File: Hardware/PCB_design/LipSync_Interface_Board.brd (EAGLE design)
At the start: 69.8 x 63.5 mm, 31 parts, among them T1 2N3906, U2 SF_MATE_RN42, U3 MPXV7002

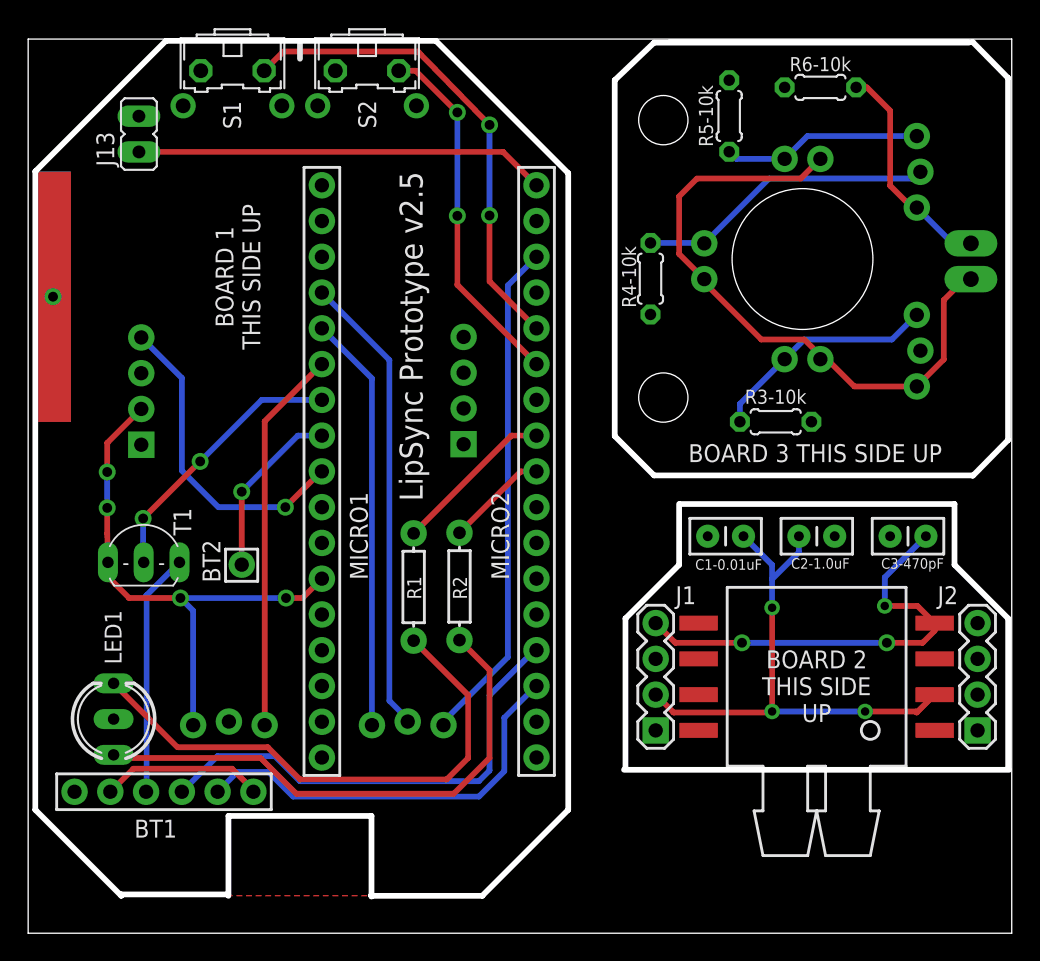
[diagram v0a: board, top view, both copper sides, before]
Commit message: Updated PCB eagle files to version 2.7
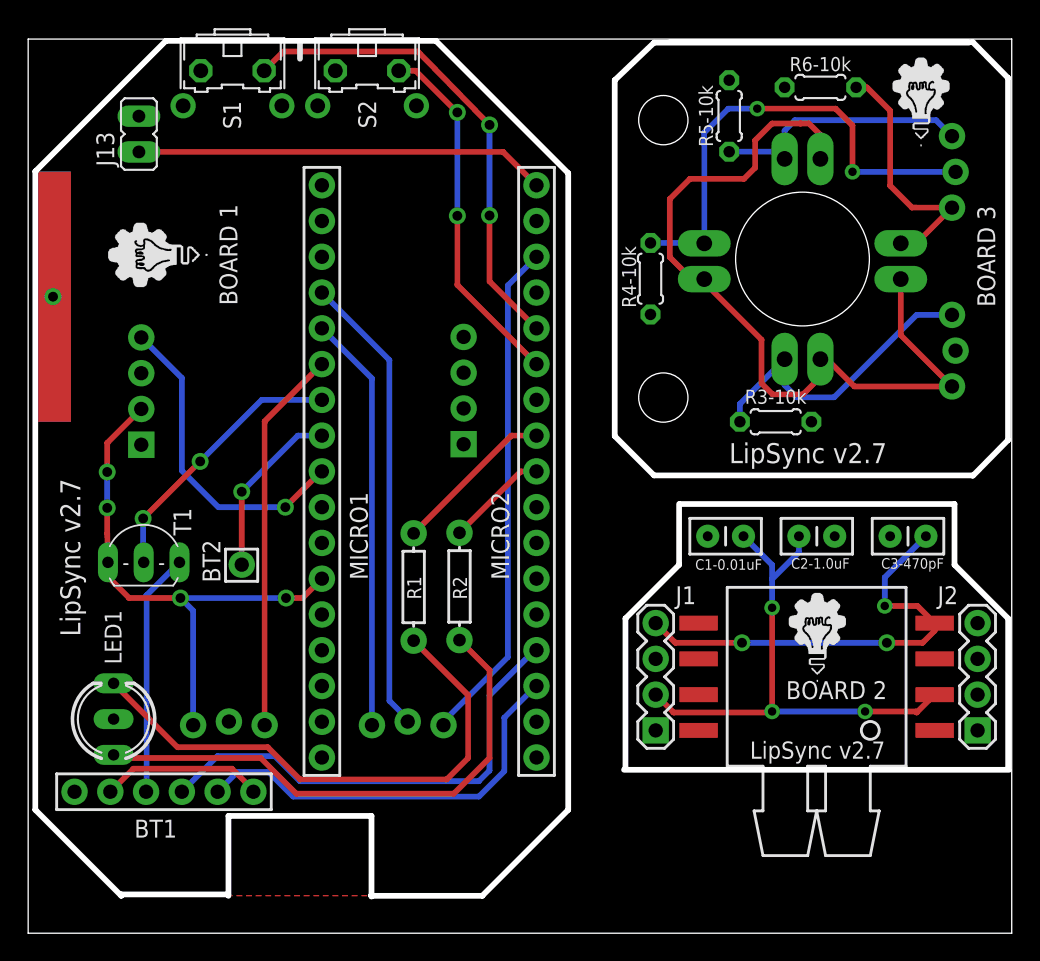
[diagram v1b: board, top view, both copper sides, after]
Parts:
- J1, J12, J2: device SparkFun-Connectors:1X02 -> SparkFun-Connectors:1X02_LONGPADS
- J10: device SparkFun-Connectors:1X02_LONGPADS -> SparkFun-Connectors:1X02_LONGPADS@1
- moved J10 4.98 mm to (62.0, 46.5)
- moved J11 2.50 mm to (65.7, 56.6)
- moved J9 2.50 mm to (65.7, 43.9)
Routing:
- net N$28: track 21.3 -> 34.0 mm, vias 0 -> 2
- net N$16: track 45.8 -> 57.7 mm
- net N$22: track 16.5 -> 22.3 mm
- net N$24: track 14.2 -> 18.8 mm
- net N$27: track 15.9 -> 18.2 mm
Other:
- board text added: "BOARD 1"
- board text added: "BOARD 2"
- board text added: "BOARD 3"
- board text added: "LipSync v2.7"
- board text removed: "BOARD 1 THIS SIDE UP"
- board text removed: "BOARD 2 THIS SIDE UP"
- board text removed: "BOARD 3 THIS SIDE UP"
- board text removed: "LipSync Prototype v2.5"

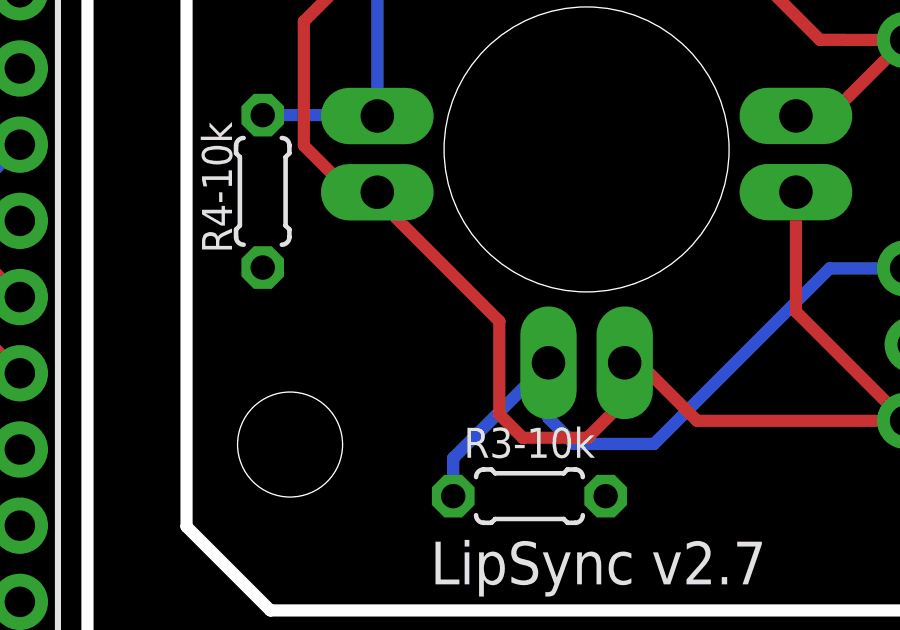
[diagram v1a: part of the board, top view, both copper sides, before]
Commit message: Updated Joystick PCB ( Reconnected a trace )
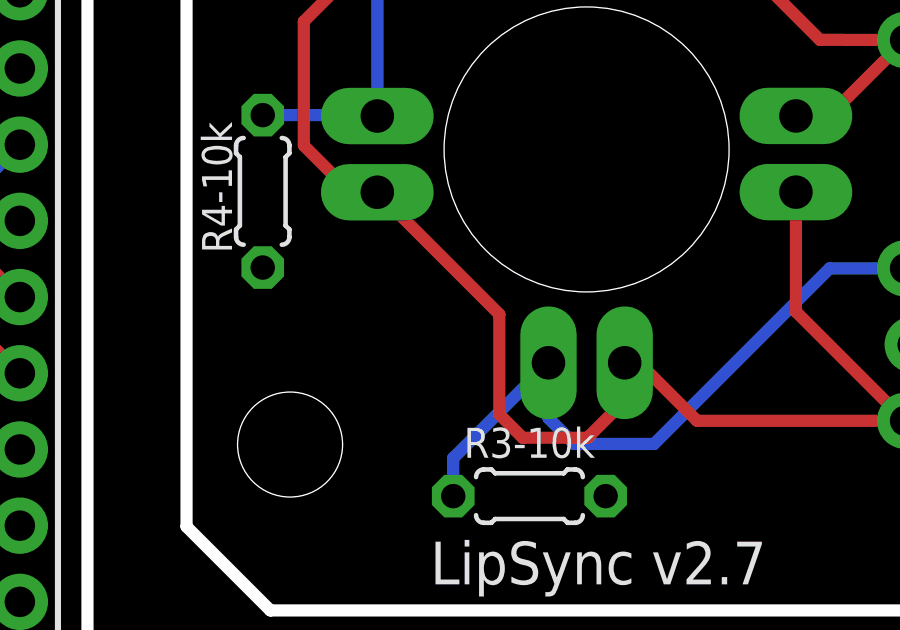
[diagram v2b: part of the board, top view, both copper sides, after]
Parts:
- J1, J2: device SparkFun-Connectors:1X02_LONGPADS -> SparkFun-Connectors:1X04
- J10: device SparkFun-Connectors:1X02_LONGPADS@1 -> SparkFun-Connectors:1X04
- J12: device SparkFun-Connectors:1X02_LONGPADS -> SparkFun-Connectors:1X03_LOCK
- J3, J4: device SparkFun-Connectors:1X04 -> SparkFun-Connectors:1X03_LOCK
- J5, J6: device SparkFun-Connectors:1X04 -> SparkFun-Connectors:1X02_LONGPADS
- J7: device SparkFun-Connectors:1X03_LOCK -> SparkFun-Connectors:1X02_LONGPADS
- J8: device SparkFun-Connectors:1X03_LOCK -> SparkFun-Connectors:1X02_LONGPADS@1
- J9: device SparkFun-Connectors:1X03_LOCK -> SparkFun-Connectors:1X04
- moved J11 68.2 mm to (11.7, 14.9), turned to 180 degrees
- moved J8 59.3 mm to (62.0, 46.5), turned to 90 degrees
- moved J3 58.4 mm to (65.7, 43.9), turned to 270 degrees
- moved J10 55.2 mm to (8.03, 34.7)
- moved J7 51.2 mm to (56.3, 55.0), turned to 0 degrees
- moved J4 42.2 mm to (65.7, 56.6), flipped to the bottom, turned to 270 degrees
- moved J2 42.1 mm to (67.4, 14.4), flipped to the top, turned to 90 degrees
- moved J12 39.4 mm to (24.4, 14.9), turned to 180 degrees
- moved J9 36.0 mm to (30.9, 34.7), turned to 90 degrees
- moved J1 28.8 mm to (44.6, 14.4), flipped to the top, turned to 90 degrees
- moved J5 28.8 mm to (56.3, 40.8), flipped to the bottom, turned to 0 degrees
- moved J6 20.7 mm to (48.0, 46.5)
- renumbered JP1 to J13
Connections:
- net GND: now also J10.3, J11.2; no longer J3.3, J8.2
- net GND2: now also J1.3; no longer J5.3
- net GND3: now also J3.2; no longer J9.2
- net N$10: now also J12.3; no longer J7.3
- net N$11: now also J10.4; no longer J3.4
- net N$16: now also J3.3, J5.1, J6.1, J7.1, J8.1; no longer J1.1, J10.1, J12.1, J2.1, J9.3
- net N$21: now also J11.3; no longer J8.3
- net N$22: now also J3.1, J5.2; no longer J1.2, J9.1
- net N$24: now also J4.1, J7.2; no longer J11.1, J2.2
- net N$27: now also J4.3, J8.2; no longer J10.2, J11.3
- net N$28: now also J4.2, J6.2; no longer J11.2, J12.2
- net N$5: now also J12.2; no longer J7.2
- net N$6: now also J12.1; no longer J7.1
- net N$7: now also J1.4; no longer J5.4
- net N$8: now also J1.2; no longer J5.2
- net VCC: now also J10.2, J11.1; no longer J3.2, J8.1

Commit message: Added PCB files Version 2.71 with updated MMC Logo.
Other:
- board size 69.8 x 63.5 mm -> 69.1 x 60.7 mm
- board text added: "LipSync v2.71"
- board text removed: "LipSync v2.7"
